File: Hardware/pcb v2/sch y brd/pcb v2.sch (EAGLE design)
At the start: 61 parts, among them J1 AVR_SPI_PRG_6PTH, J2 1981584-1, J3 HDMI, J4 HDMI, Q1 PMBT3904, Q2 PMBT3904, Q3 32.768kHz 12.5pF, U1 ATMEGA328P, U2 TXS0108EPWR-TSSOP20, U3 MB85RS16N, U4 ADP3338AKCZ-3.3RL7, U5 DS1307SO8, Y1 16Mhz

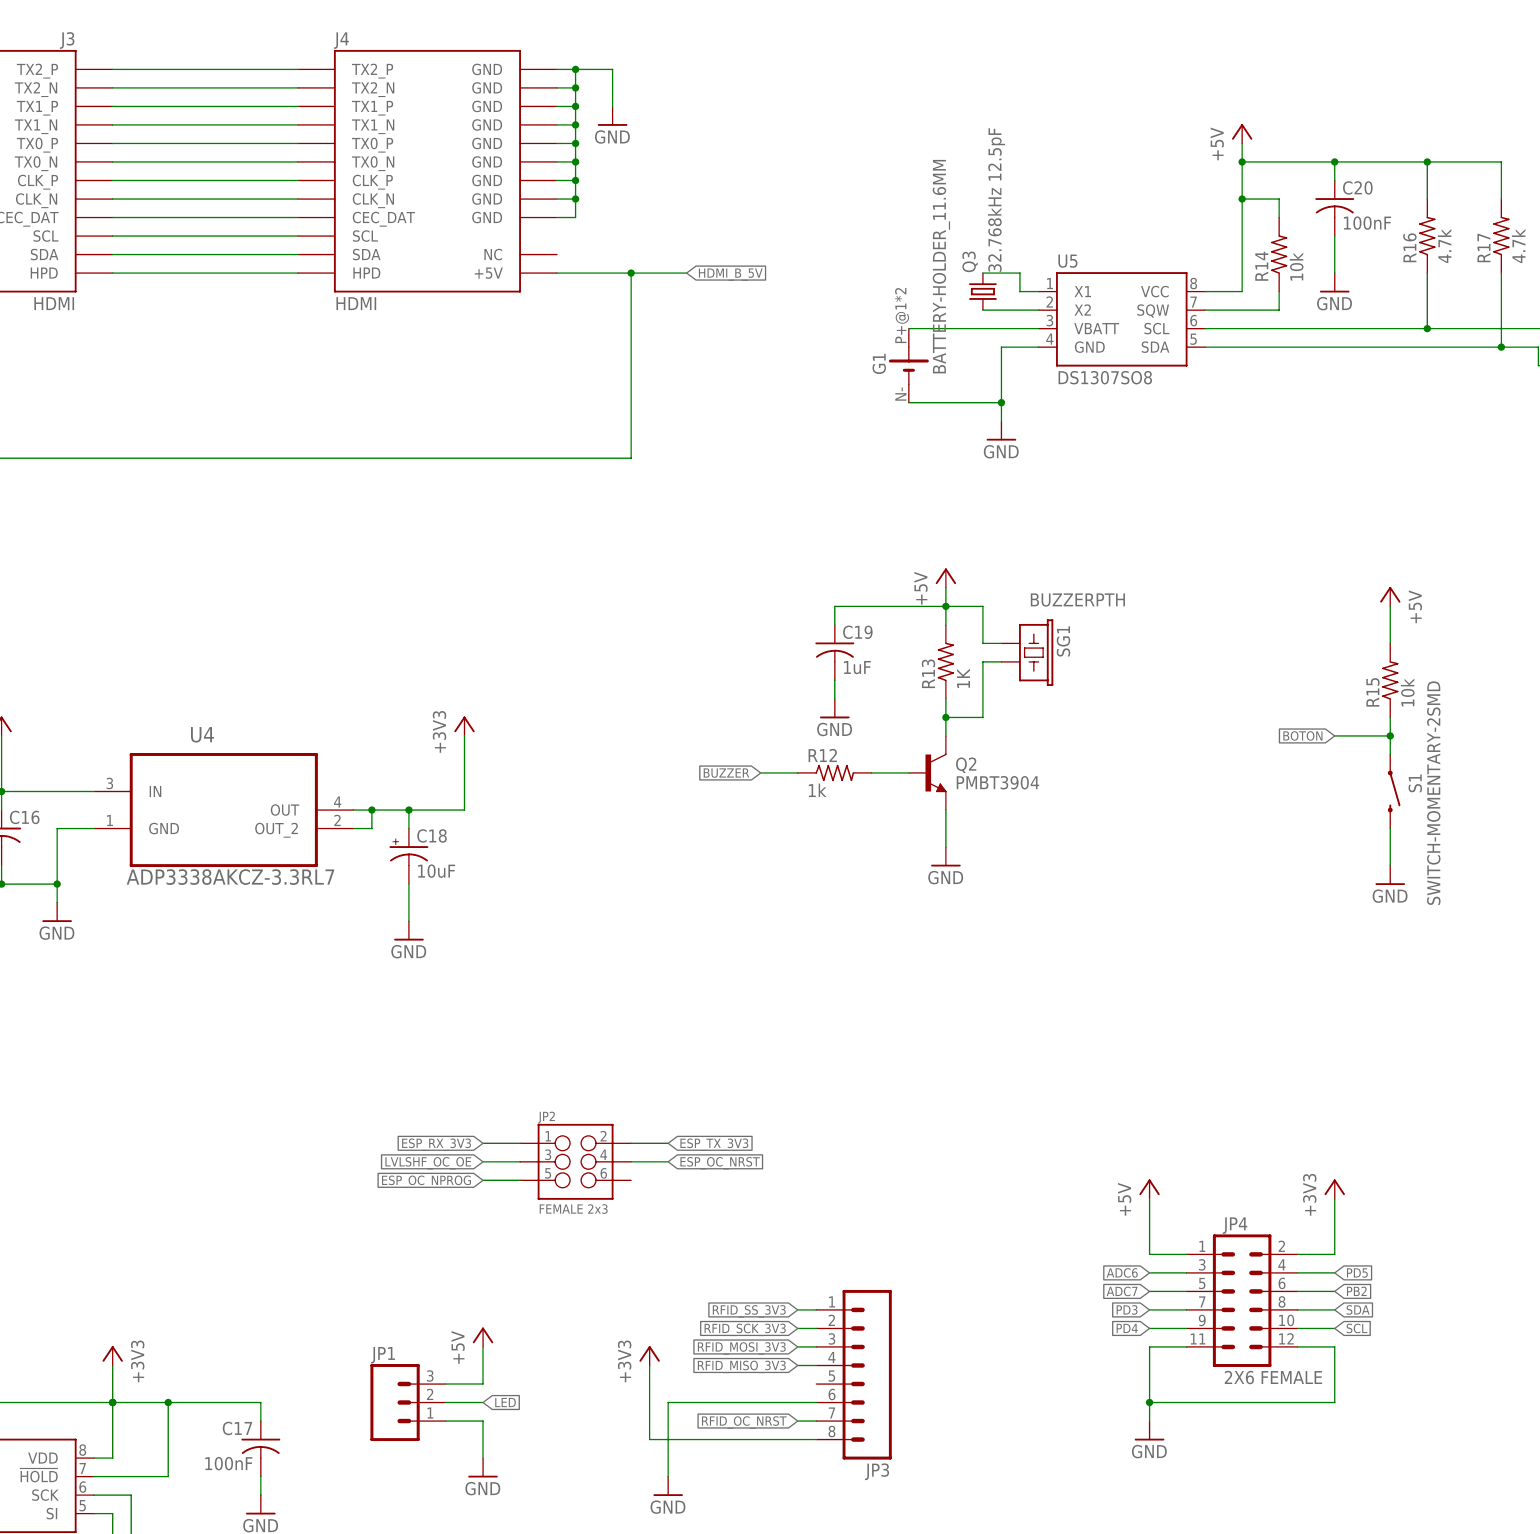
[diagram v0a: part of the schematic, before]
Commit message: Comienzo ruteo
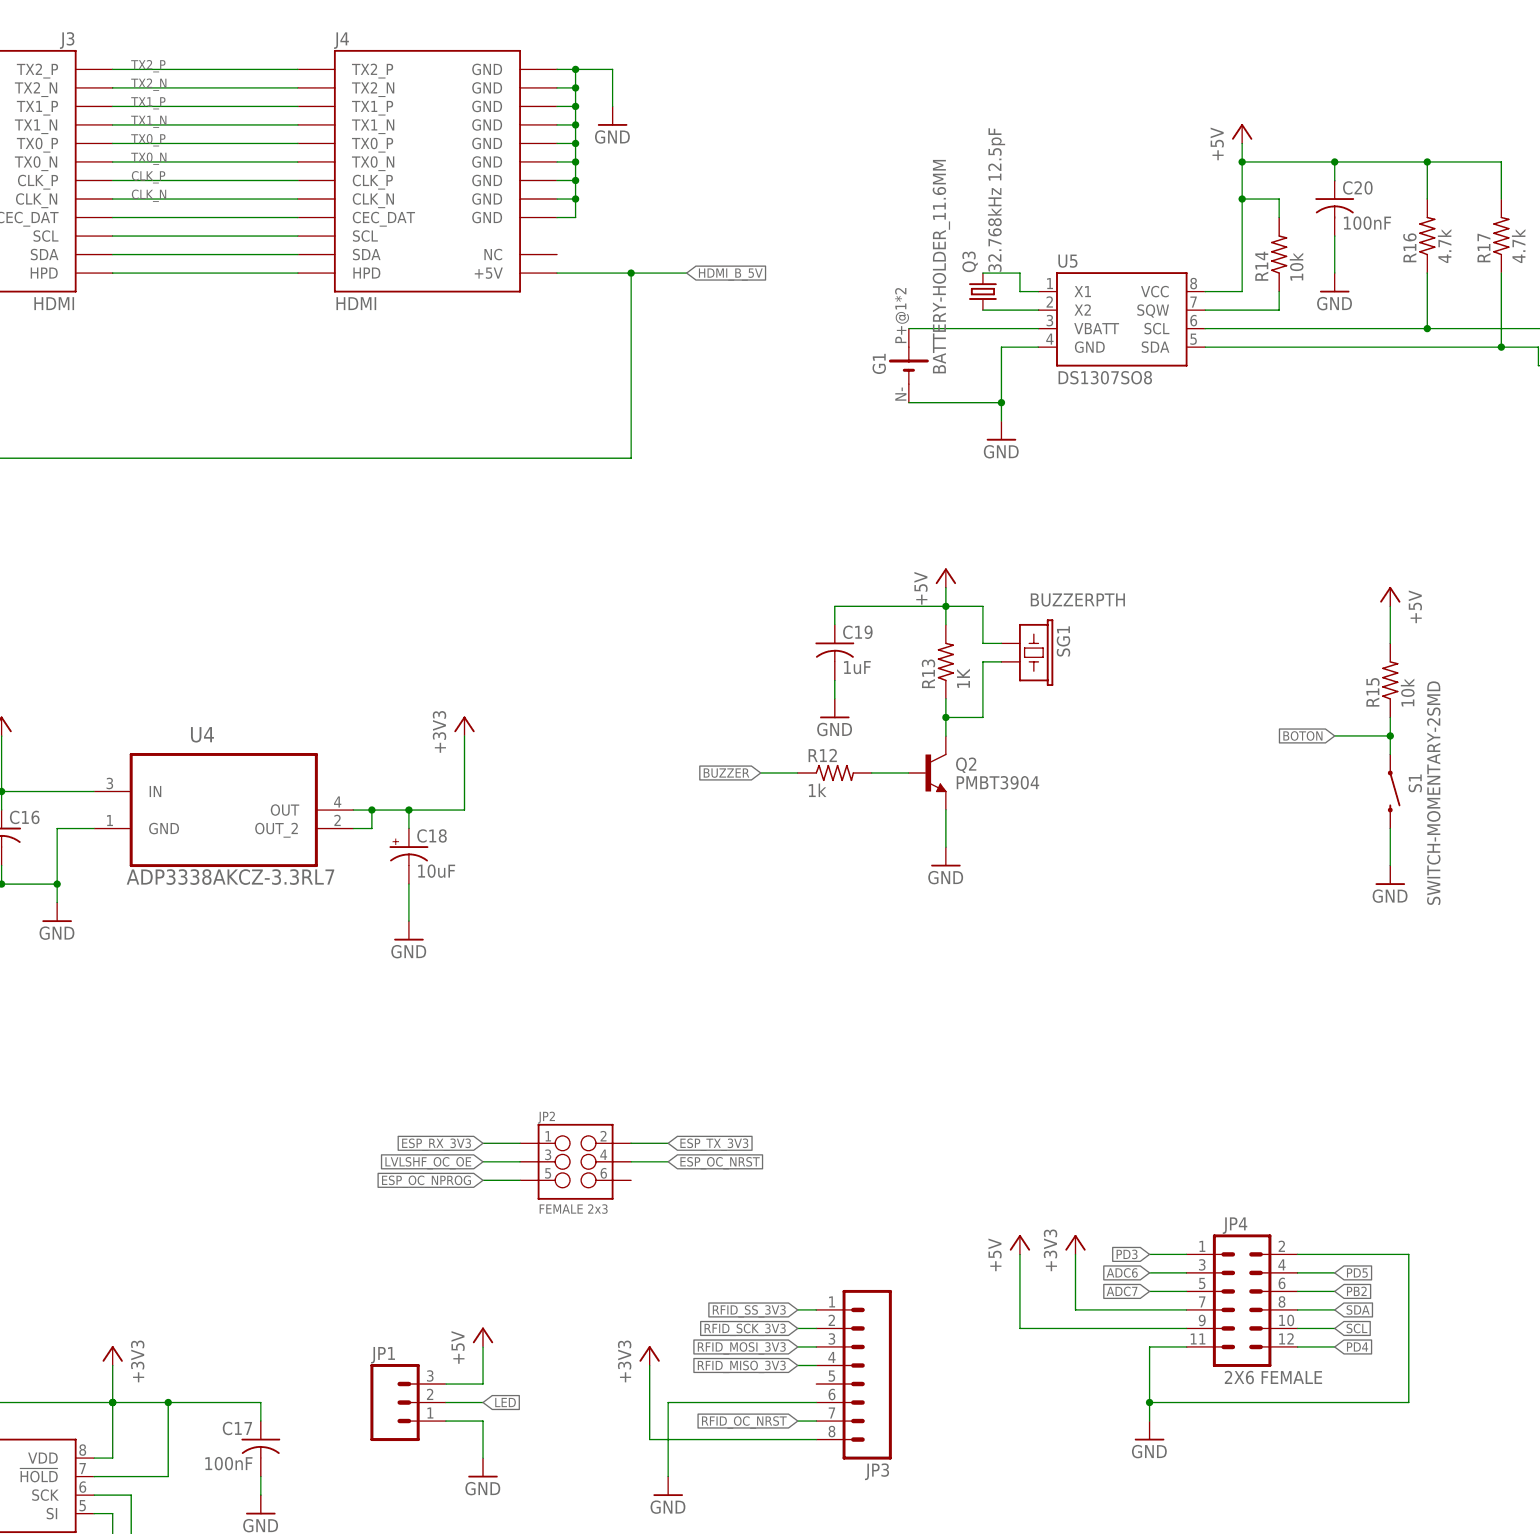
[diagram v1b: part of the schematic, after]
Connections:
- net N$23 renamed TX2_N
- net N$24 renamed TX1_P
- net N$25 renamed TX1_N
- net N$26 renamed TX0_P
- net N$27 renamed TX0_N
- net N$28 renamed CLK_P
- net N$29 renamed CLK_N
- net N$9 renamed TX2_P
- net +3V3: now also JP4.7; no longer JP4.2
- net +5V: now also JP4.9; no longer JP4.1
- net GND: now also JP4.2; no longer JP4.12
- net PD3: now also JP4.1; no longer JP4.7
- net PD4: now also JP4.12; no longer JP4.9
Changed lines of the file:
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@@
 <clearance class="3" value="0.254"/>
+</class>
+<class number="4" name="hdmi" width="2.54" drill="0">
 </class>
 <class number="6" name="1V8" width="0.254" drill="0.3">
@@
 <instance part="JP4" gate="G$1" x="419.1" y="17.78"/>
 <instance part="GND23" gate="1" x="408.94" y="5.08"/>
-<instance part="P+8" gate="1" x="408.94" y="40.64"/>
-<instance part="+3V38" gate="G$1" x="434.34" y="40.64"/>
+<instance part="P+8" gate="1" x="391.16" y="33.02"/>
+<instance part="+3V38" gate="G$1" x="398.78" y="33.02"/>
 <instance part="JP1" gate="G$1" x="304.8" y="10.16"/>
 <instance part="P+6" gate="1" x="317.5" y="20.32"/>
@@
 <pinref part="GND23" gate="1" pin="GND"/>
 <wire x1="408.94" y1="7.62" x2="408.94" y2="10.16" width="0.1524" layer="91"/>
-<pinref part="JP4" gate="G$1" pin="12"/>
 <wire x1="408.94" y1="10.16" x2="408.94" y2="17.78" width="0.1524" layer="91"/>
-<wire x1="429.26" y1="17.78" x2="434.34" y2="17.78" width="0.1524" layer="91"/>
-<wire x1="434.34" y1="17.78" x2="434.34" y2="10.16" width="0.1524" layer="91"/>
-<wire x1="434.34" y1="10.16" x2="408.94" y2="10.16" width="0.1524" layer="91"/>
+<wire x1="444.5" y1="10.16" x2="408.94" y2="10.16" width="0.1524" layer="91"/>
 <junction x="408.94" y="10.16"/>
+<wire x1="444.5" y1="10.16" x2="444.5" y2="30.48" width="0.1524" layer="91"/>
+<pinref part="JP4" gate="G$1" pin="2"/>
+<wire x1="444.5" y1="30.48" x2="429.26" y2="30.48" width="0.1524" layer="91"/>
 </segment>
 <segment>
@@
 </segment>
 <segment>
-<pinref part="JP4" gate="G$1" pin="1"/>
-<wire x1="414.02" y1="30.48" x2="408.94" y2="30.48" width="0.1524" layer="91"/>
-<pinref part="P+8" gate="1" pin="+5V"/>
-<wire x1="408.94" y1="30.48" x2="408.94" y2="38.1" width="0.1524" layer="91"/>
-</segment>
-<segment>
 <pinref part="JP1" gate="G$1" pin="3"/>
 <wire x1="312.42" y1="12.7" x2="317.5" y2="12.7" width="0.1524" layer="91"/>
 <wire x1="317.5" y1="12.7" x2="317.5" y2="17.78" width="0.1524" layer="91"/>
 <pinref part="P+6" gate="1" pin="+5V"/>
+</segment>
+<segment>
+<pinref part="JP4" gate="G$1" pin="9"/>
+<pinref part="P+8" gate="1" pin="+5V"/>
+<wire x1="414.02" y1="20.32" x2="391.16" y2="20.32" width="0.1524" layer="91"/>
+<wire x1="391.16" y1="20.32" x2="391.16" y2="30.48" width="0.1524" layer="91"/>
 </segment>
 </net>
@@
 </segment>
 <segment>
-<pinref part="JP4" gate="G$1" pin="2"/>
-<wire x1="429.26" y1="30.48" x2="434.34" y2="30.48" width="0.1524" layer="91"/>
 <pinref part="+3V38" gate="G$1" pin="+3V3"/>
-<wire x1="434.34" y1="30.48" x2="434.34" y2="38.1" width="0.1524" layer="91"/>
+<wire x1="398.78" y1="30.48" x2="398.78" y2="22.86" width="0.1524" layer="91"/>
+<pinref part="JP4" gate="G$1" pin="7"/>
+<wire x1="398.78" y1="22.86" x2="414.02" y2="22.86" width="0.1524" layer="91"/>
 </segment>
 </net>
@@
 </segment>
 </net>
-<net name="N$9" class="0">
+<net name="TX2_P" class="4">
 <segment>
 <pinref part="J3" gate="G$1" pin="TX2_P"/>
 <pinref part="J4" gate="G$1" pin="TX2_P"/>
 <wire x1="266.7" y1="193.04" x2="292.1" y2="193.04" width="0.1524" layer="91"/>
-</segment>
-</net>
-<net name="N$23" class="0">
+<label x="269.24" y="193.04" size="1.27" layer="95"/>
+</segment>
+</net>
+<net name="TX2_N" class="4">
 <segment>
 <pinref part="J3" gate="G$1" pin="TX2_N"/>
 <pinref part="J4" gate="G$1" pin="TX2_N"/>
 <wire x1="266.7" y1="190.5" x2="292.1" y2="190.5" width="0.1524" layer="91"/>
-</segment>
-</net>
-<net name="N$24" class="0">
+<label x="269.24" y="190.5" size="1.27" layer="95"/>
+</segment>
+</net>
+<net name="TX1_P" class="4">
 <segment>
 <pinref part="J3" gate="G$1" pin="TX1_P"/>
 <pinref part="J4" gate="G$1" pin="TX1_P"/>
 <wire x1="266.7" y1="187.96" x2="292.1" y2="187.96" width="0.1524" layer="91"/>
-</segment>
-</net>
-<net name="N$25" class="0">
+<label x="269.24" y="187.96" size="1.27" layer="95"/>
+</segment>
+</net>
+<net name="TX1_N" class="4">
 <segment>
 <pinref part="J3" gate="G$1" pin="TX1_N"/>
 <pinref part="J4" gate="G$1" pin="TX1_N"/>
 <wire x1="266.7" y1="185.42" x2="292.1" y2="185.42" width="0.1524" layer="91"/>
-</segment>
-</net>
-<net name="N$26" class="0">
+<label x="269.24" y="185.42" size="1.27" layer="95"/>
+</segment>
+</net>
+<net name="TX0_P" class="4">
 <segment>
 <pinref part="J3" gate="G$1" pin="TX0_P"/>
 <pinref part="J4" gate="G$1" pin="TX0_P"/>
 <wire x1="266.7" y1="182.88" x2="292.1" y2="182.88" width="0.1524" layer="91"/>
-</segment>
-</net>
-<net name="N$27" class="0">
+<label x="269.24" y="182.88" size="1.27" layer="95"/>
+</segment>
+</net>
+<net name="TX0_N" class="4">
 <segment>
 <pinref part="J3" gate="G$1" pin="TX0_N"/>
 <pinref part="J4" gate="G$1" pin="TX0_N"/>
 <wire x1="266.7" y1="180.34" x2="292.1" y2="180.34" width="0.1524" layer="91"/>
-</segment>
-</net>
-<net name="N$28" class="0">
+<label x="269.24" y="180.34" size="1.27" layer="95"/>
+</segment>
+</net>
+<net name="CLK_P" class="4">
 <segment>
 <pinref part="J3" gate="G$1" pin="CLK_P"/>
 <pinref part="J4" gate="G$1" pin="CLK_P"/>
 <wire x1="266.7" y1="177.8" x2="292.1" y2="177.8" width="0.1524" layer="91"/>
-</segment>
-</net>
-<net name="N$29" class="0">
+<label x="269.24" y="177.8" size="1.27" layer="95"/>
+</segment>
+</net>
+<net name="CLK_N" class="4">
 <segment>
 <pinref part="J3" gate="G$1" pin="CLK_N"/>
 <pinref part="J4" gate="G$1" pin="CLK_N"/>
 <wire x1="266.7" y1="175.26" x2="292.1" y2="175.26" width="0.1524" layer="91"/>
+<label x="269.24" y="175.26" size="1.27" layer="95"/>
 </segment>
 </net>
@@
 </segment>
 <segment>
-<pinref part="JP4" gate="G$1" pin="7"/>
-<wire x1="414.02" y1="22.86" x2="408.94" y2="22.86" width="0.1524" layer="91"/>
-<label x="408.94" y="22.86" size="1.27" layer="95" rot="R180" xref="yes"/>
+<pinref part="JP4" gate="G$1" pin="1"/>
+<wire x1="414.02" y1="30.48" x2="408.94" y2="30.48" width="0.1524" layer="91"/>
+<label x="408.94" y="30.48" size="1.27" layer="95" rot="R180" xref="yes"/>
 </segment>
 </net>
@@
 </segment>
 <segment>
-<pinref part="JP4" gate="G$1" pin="9"/>
-<wire x1="414.02" y1="20.32" x2="408.94" y2="20.32" width="0.1524" layer="91"/>
-<label x="408.94" y="20.32" size="1.27" layer="95" rot="R180" xref="yes"/>
-</segment>
-</net>
+<pinref part="JP4" gate="G$1" pin="12"/>
+<wire x1="429.26" y1="17.78" x2="434.34" y2="17.78" width="0.1524" layer="91"/>
+<label x="434.34" y="17.78" size="1.27" layer="95" xref="yes"/>
+</segment>
+</net>

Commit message: empaquetados
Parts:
- removed C18: 10uF, rcl:CPOL-USE2.5-6
- removed G1: BATTERY-HOLDER_11.6MM, battery:BATTERY-HOLDER_11.6MM
- removed Q3: 32.768kHz 12.5pF, crystal:CRYSTALTC26H
- removed SG1: BUZZERPTH, SparkFun-Electromechanical:BUZZERPTH
- removed Y1: 16Mhz, SparkFun-FreqCtrl:CRYSTALHC49US
- added CN1: (no value), adafruit:JST_2PIN-SMT
- added Q4: MC-306, crystal:MC-306
- added SP1: SPEAKER/PS12, adafruit:SPEAKER/PS12
- added U6: BATTERYBATTERY1225_SMT, seeedleo:BATTERYBATTERY1225_SMT
- added Y2: CSTCE16M0V53-R0 16MHZ, SmartPrj:RESONATORMU
- C15: value 10uF -> 1000uF; device rcl:CPOL-USE2.5-6 -> rcl:CPOL-USUD-10X10
- C16: value 1000uF -> (none); device rcl:CPOL-USE2.5-6 -> rcl:CPOL-USUD-5X5,8
- C5: value 22pF -> 1000uF; device rcl:C-USC1206 -> rcl:CPOL-USUD-10X10
- C6: value 22pF -> 100uF; device rcl:C-USC1206 -> rcl:C-USC0805
- J2: MF Hirose -> (none); MPN ZX62-AB-5PA(11) -> (none)
- R14: value 10k -> 4.7k
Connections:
- removed net N$12: C6.1, U1.PB7(XTAL2/TOSC2), Y1.2
- new net N$9: U5.VBATT, U6.+
- net +3V3: now also C16.+; no longer C18.+
- net +5V: now also C5.+, C6.1, SP1.+; no longer C16.+, SG1.1
- net GND: now also C5.-, JP2.6, U6.-, Y2.2; no longer C18.-, C5.2, G1.-
- net N$11: now also Y2.1; no longer C5.1, Y1.1
- net N$2: now also Q4.2; no longer Q3.2
- net N$3: now also Q4.1; no longer Q3.1
- net N$4: now also U1.PB7(XTAL2/TOSC2), Y2.3; no longer G1.+, U5.VBATT
- net N$5: now also SP1.-; no longer SG1.2
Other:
- moved on the sheet: C15, C16, C6
